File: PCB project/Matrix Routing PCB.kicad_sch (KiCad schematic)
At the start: 14 parts, among them J1 Connector 1x6, J2 JST_PH_S4B-PH-SM4-TB_1x04-1MP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, J3 ESQ-105-11-T-D, J4 TSM-102-01-L-DH-A, J5 USB-A-S-X-X-SM2-R, U1 FT232RL

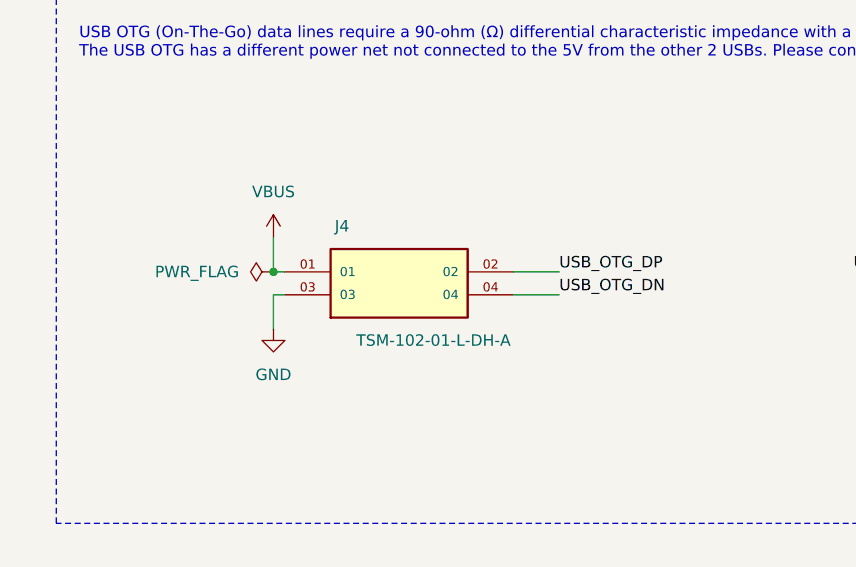
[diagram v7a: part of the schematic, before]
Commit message: Adding the netclasses, and physical board and track and gap
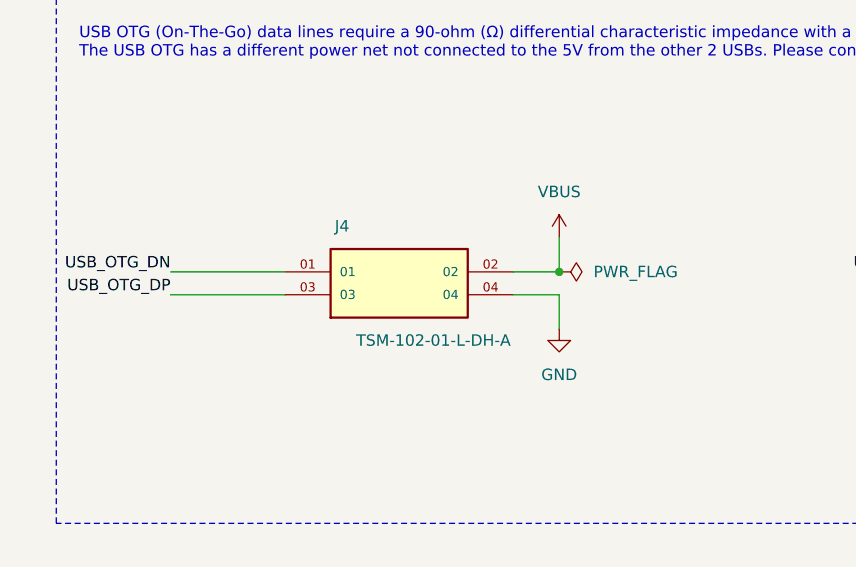
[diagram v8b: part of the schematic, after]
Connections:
- net GND: now also J4.04; no longer J4.03
- net USB_OTG_DN: now also J4.01; no longer J4.04
- net USB_OTG_DP: now also J4.03; no longer J4.02
- net VBUS: now also J4.02; no longer J4.01
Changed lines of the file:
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@@
 	)
 	(junction
-		(at 100.33 200.66)
+		(at 228.6 54.61)
 		(diameter 0)
 		(color 0 0 0 0)
 	)
 	(junction
-		(at 228.6 54.61)
+		(at 132.08 200.66)
 		(diameter 0)
 		(color 0 0 0 0)
@@
 	(wire
 		(pts
-			(xy 101.6 200.66) (xy 100.33 200.66)
-		)
-		(stroke
-			(width 0)
-			(type default)
-		)
-	)
-	(wire
-		(pts
 			(xy 212.09 54.61) (xy 212.09 55.88)
 		)
@@
 	(wire
 		(pts
-			(xy 100.33 203.2) (xy 101.6 203.2)
+			(xy 127 200.66) (xy 132.08 200.66)
 		)
 		(stroke
@@
 	(wire
 		(pts
+			(xy 132.08 196.85) (xy 132.08 200.66)
+		)
+		(stroke
+			(width 0)
+			(type default)
+		)
+	)
+	(wire
+		(pts
+			(xy 88.9 200.66) (xy 101.6 200.66)
+		)
+		(stroke
+			(width 0)
+			(type default)
+		)
+	)
+	(wire
+		(pts
 			(xy 82.55 76.2) (xy 105.41 76.2)
 		)
@@
 	(wire
 		(pts
-			(xy 132.08 203.2) (xy 127 203.2)
-		)
-		(stroke
-			(width 0)
-			(type default)
-		)
-	)
-	(wire
-		(pts
 			(xy 102.87 68.58) (xy 105.41 68.58)
 		)
@@
 	(wire
 		(pts
-			(xy 100.33 203.2) (xy 100.33 207.01)
+			(xy 177.8 73.66) (xy 177.8 77.47)
 		)
 		(stroke
@@
 	(wire
 		(pts
-			(xy 177.8 73.66) (xy 177.8 77.47)
+			(xy 210.82 73.66) (xy 177.8 73.66)
 		)
 		(stroke
@@
 	(wire
 		(pts
-			(xy 210.82 73.66) (xy 177.8 73.66)
+			(xy 88.9 203.2) (xy 101.6 203.2)
 		)
 		(stroke
@@
 	(wire
 		(pts
-			(xy 100.33 200.66) (xy 100.33 196.85)
+			(xy 233.68 118.11) (xy 236.22 118.11)
 		)
 		(stroke
@@
 	(wire
 		(pts
-			(xy 233.68 118.11) (xy 236.22 118.11)
+			(xy 118.11 71.12) (xy 128.27 71.12)
 		)
 		(stroke
@@
 	(wire
 		(pts
-			(xy 118.11 71.12) (xy 128.27 71.12)
+			(xy 195.58 83.82) (xy 210.82 83.82)
 		)
 		(stroke
@@
 	(wire
 		(pts
-			(xy 195.58 83.82) (xy 210.82 83.82)
+			(xy 132.08 203.2) (xy 132.08 207.01)
 		)
 		(stroke
@@
 	(wire
 		(pts
-			(xy 186.69 210.82) (xy 186.69 205.74)
+			(xy 127 203.2) (xy 132.08 203.2)
 		)
 		(stroke
@@
 	(wire
 		(pts
-			(xy 127 200.66) (xy 132.08 200.66)
+			(xy 186.69 210.82) (xy 186.69 205.74)
 		)
 		(stroke
@@
 	)
 	(label "USB_OTG_DP"
-		(at 132.08 200.66 0)
+		(at 88.9 203.2 180)
 		(effects
 			(font
 				(size 1.27 1.27)
 			)
-			(justify left bottom)
+			(justify right bottom)
 		)
 	)
@@
 	)
 	(label "USB_OTG_DN"
-		(at 132.08 203.2 0)
+		(at 88.9 200.66 180)
 		(effects
 			(font
 				(size 1.27 1.27)
 			)
-			(justify left bottom)
+			(justify right bottom)
 		)
 	)
@@
 	(symbol
 		(lib_id "power:PWR_FLAG")
-		(at 100.33 200.66 90)
+		(at 132.08 200.66 270)
+		(mirror x)
 		(unit 1)
 		(body_style 1)
@@
 		(fields_autoplaced yes)
 		(property "Reference" "#FLG2"
-			(at 98.425 200.66 0)
+			(at 133.985 200.66 0)
 			(hide yes)
 			(show_name no)
@@
 		)
 		(property "Value" "PWR_FLAG"
-			(at 96.52 200.6599 90)
+			(at 135.89 200.6599 90)
 			(show_name no)
 			(do_not_autoplace no)
@@
 		)
 		(property "Footprint" ""
-			(at 100.33 200.66 0)
+			(at 132.08 200.66 0)
 			(hide yes)
 			(show_name no)
@@
 		)
 		(property "Datasheet" ""
-			(at 100.33 200.66 0)
+			(at 132.08 200.66 0)
 			(hide yes)
 			(show_name no)
@@
 		)
 		(property "Description" "Special symbol for telling ERC where power comes from"
-			(at 100.33 200.66 0)
+			(at 132.08 200.66 0)
 			(hide yes)
 			(show_name no)
@@
 	(symbol
 		(lib_id "power:GND")
-		(at 100.33 207.01 0)
+		(at 132.08 207.01 0)
+		(mirror y)
 		(unit 1)
 		(body_style 1)
@@
 		(fields_autoplaced yes)
 		(property "Reference" "#PWR8"
-			(at 100.33 213.36 0)
+			(at 132.08 213.36 0)
 			(hide yes)
 			(show_name no)
@@
 		)
 		(property "Value" "GND"
-			(at 100.33 212.09 0)
+			(at 132.08 212.09 0)
 			(show_name no)
 			(do_not_autoplace no)
@@
 		)
 		(property "Footprint" ""
-			(at 100.33 207.01 0)
+			(at 132.08 207.01 0)
 			(hide yes)
 			(show_name no)
@@
 		)
 		(property "Datasheet" ""
-			(at 100.33 207.01 0)
+			(at 132.08 207.01 0)
 			(hide yes)
 			(show_name no)
@@
 		)
 		(property "Description" "Power symbol creates a global label with name \"GND\" , ground"
-			(at 100.33 207.01 0)
+			(at 132.08 207.01 0)
 			(hide yes)
 			(show_name no)
@@
 	(symbol
 		(lib_id "power:VBUS")
-		(at 100.33 196.85 0)
+		(at 132.08 196.85 0)
+		(mirror y)
 		(unit 1)
 		(body_style 1)
@@
 		(fields_autoplaced yes)
 		(property "Reference" "#PWR9"
-			(at 100.33 200.66 0)
+			(at 132.08 200.66 0)
 			(hide yes)
 			(show_name no)
@@
 		)
 		(property "Value" "VBUS"
-			(at 100.33 191.77 0)
+			(at 132.08 191.77 0)
 			(show_name no)
 			(do_not_autoplace no)
@@
 		)
 		(property "Footprint" ""
-			(at 100.33 196.85 0)
+			(at 132.08 196.85 0)
 			(hide yes)
 			(show_name no)
@@
 		)
 		(property "Datasheet" ""
-			(at 100.33 196.85 0)
+			(at 132.08 196.85 0)
 			(hide yes)
 			(show_name no)
@@
 		)
 		(property "Description" "Power symbol creates a global label with name \"VBUS\""
-			(at 100.33 196.85 0)
+			(at 132.08 196.85 0)
 			(hide yes)
 			(show_name no)
